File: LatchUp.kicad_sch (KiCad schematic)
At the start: 25 parts, among them Q10 IRF7406, Q11 BSL307SP, Q9 BSS138, U25 INA138NA_3K, U26 AD589JRZ, U27 LT1636CMS8_PBF

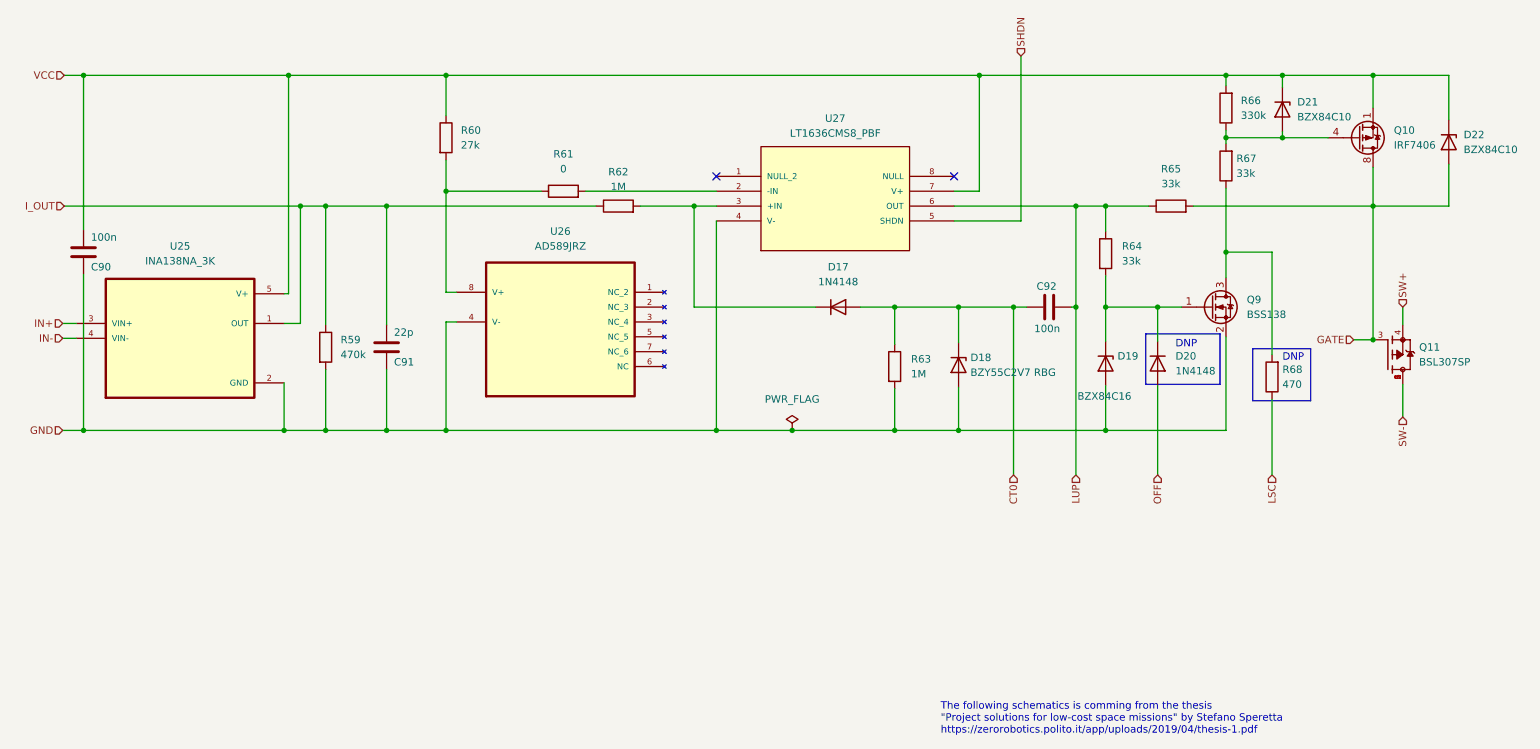
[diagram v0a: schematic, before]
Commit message: Add a defined state (pulled to GND) of the output of LT1336 for the case when it is a shutdown state
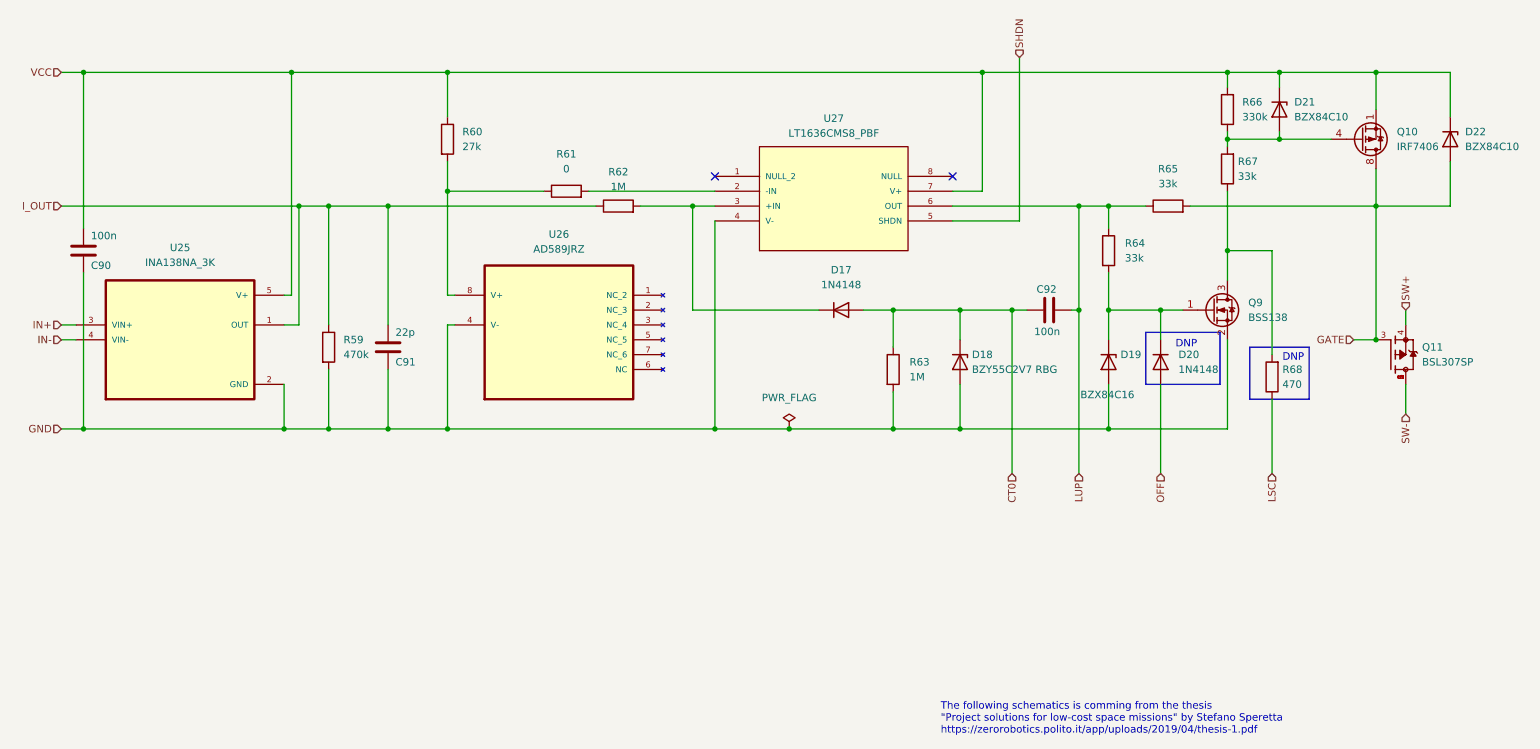
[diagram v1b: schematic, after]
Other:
- moved on the sheet: C92, D17, D18, D19, D20, D21, D22, Q10, Q11, Q9, R59, R61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

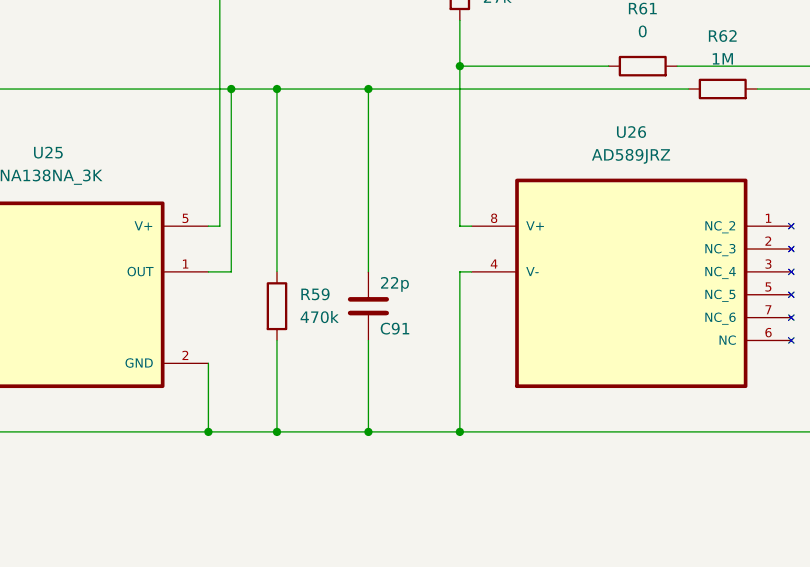
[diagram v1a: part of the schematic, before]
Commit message: Increase inrush current threshold for latch-up protection: C87, C91 22 pF -> 100 nF
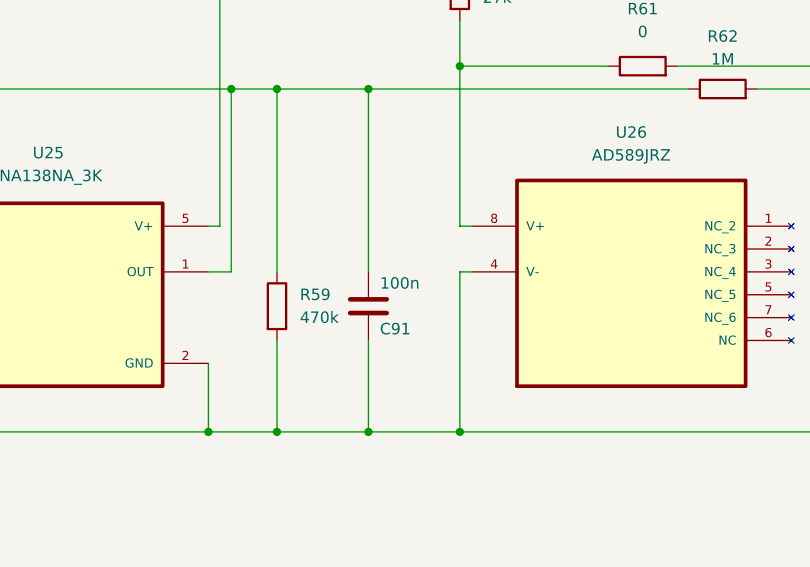
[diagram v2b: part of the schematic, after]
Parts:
- C91: value 22p -> 100n; JLCPCB Part # C3876314 -> C1591; Manufacturer_Part_Number CL10C220JB8NNWC -> CL10B104KB8NNNC
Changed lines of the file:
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@@
       (effects (font (size 1.27 1.27)) (justify right))
     )
-    (property "Value" "22p" (id 1) (at 83.82 95.25 0)
+    (property "Value" "100n" (id 1) (at 83.82 95.25 0)
       (effects (font (size 1.27 1.27)) (justify right))
     )
@@
       (effects (font (size 1.27 1.27)) hide)
     )
-    (property "JLCPCB Part #" "C3876314" (id 4) (at 82.55 97.79 0)
+    (property "JLCPCB Part #" "C1591" (id 4) (at 82.55 97.79 0)
       (effects (font (size 1.27 1.27)) hide)
     )
-    (property "Manufacturer_Part_Number" "CL10C220JB8NNWC " (id 5) (at 82.55 97.79 0)
+    (property "Manufacturer_Part_Number" "CL10B104KB8NNNC " (id 5) (at 82.55 97.79 0)
       (effects (font (size 1.27 1.27)) hide)
     )

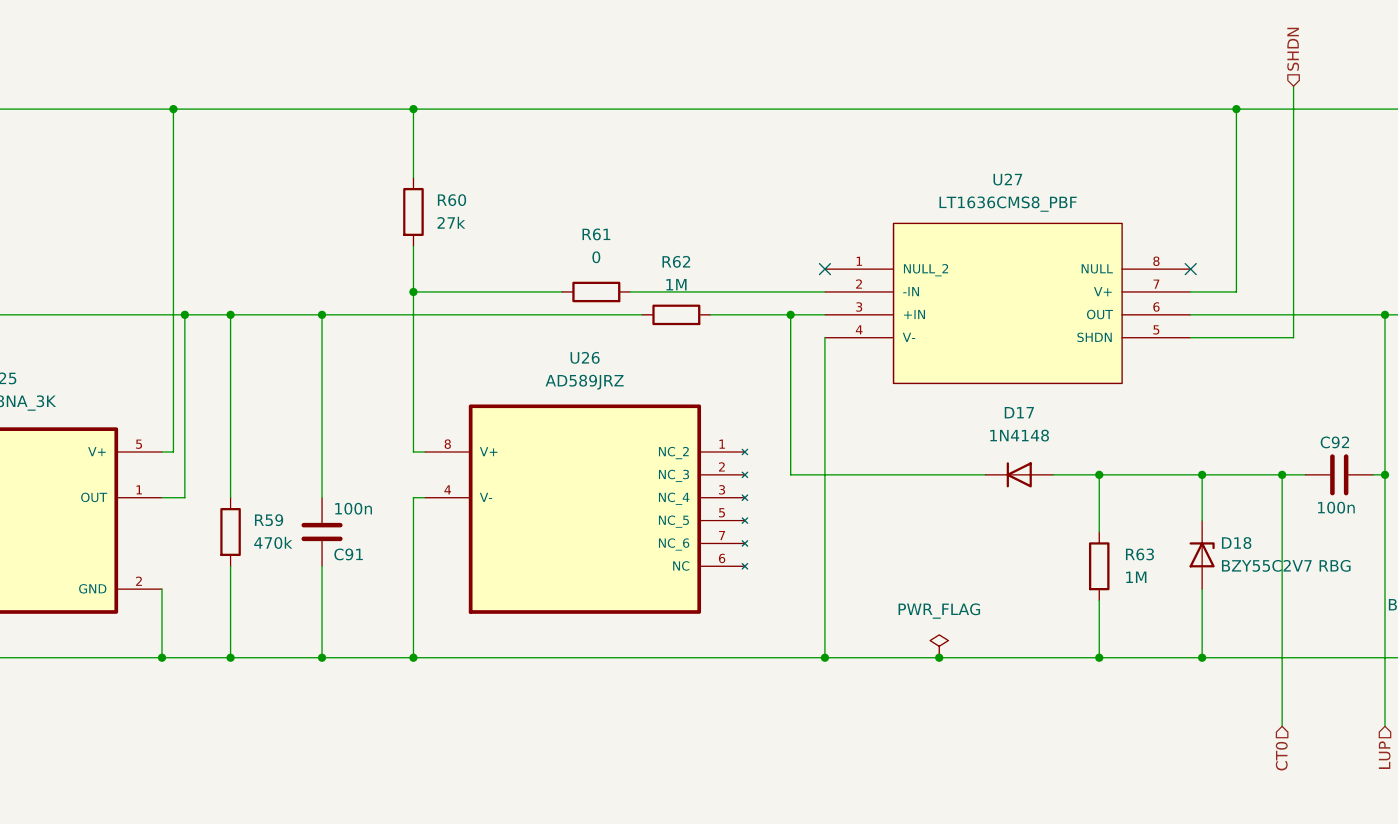
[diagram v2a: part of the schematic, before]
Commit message: Adhere to the recommendations from AD589 datasheet: R42, R80 27k -> 6.8k for ~500 uA current and add 1 nF shunt capacitor
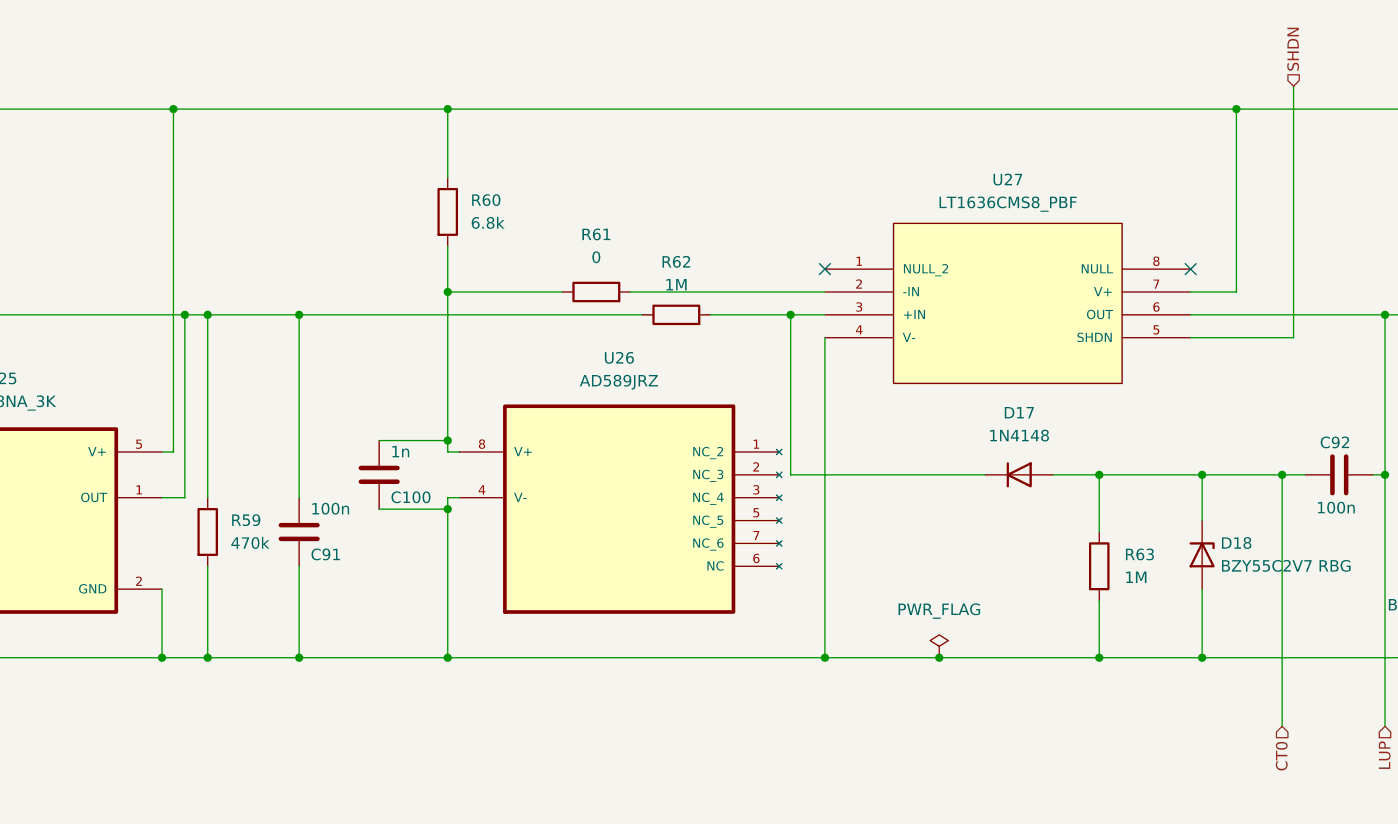
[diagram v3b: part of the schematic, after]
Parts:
- added C100: 1n, Capacitor_SMD:C_0603_1608Metric, symbol Device:C
- R60: value 27k -> 6.8k; JLCPCB Part # C4247597 -> (none); Manufacturer_Part_Number ERJ-H3EF2702V -> (none)
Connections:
- net GND: now also C100.1
- net at R60.2, R61.1, U26.8 (V+): now also C100.2
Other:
- moved on the sheet: C91, R59, R60, U26

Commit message: Update the 12 MHz crystal oscillator value and change the related capacitors: C13, C14 20 pF -> 13 pF
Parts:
- renumbered C100 to C101
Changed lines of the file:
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@@
   (symbol (lib_id "Device:C") (at 88.9 91.44 180) (unit 1)
     (in_bom yes) (on_board yes)
-    (property "Reference" "C100" (id 0) (at 90.17 93.98 0)
+    (property "Reference" "C101" (id 0) (at 90.17 93.98 0)
       (effects (font (size 1.27 1.27)) (justify right))
     )
